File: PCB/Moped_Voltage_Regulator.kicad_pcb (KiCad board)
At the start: 2 copper layers, 42.4 x 32.4 mm, 15 parts, among them J1 Screw_Terminal_01x02, J2 Screw_Terminal_01x02, Q1 IRLZ44N, Q2 IRLZ44N

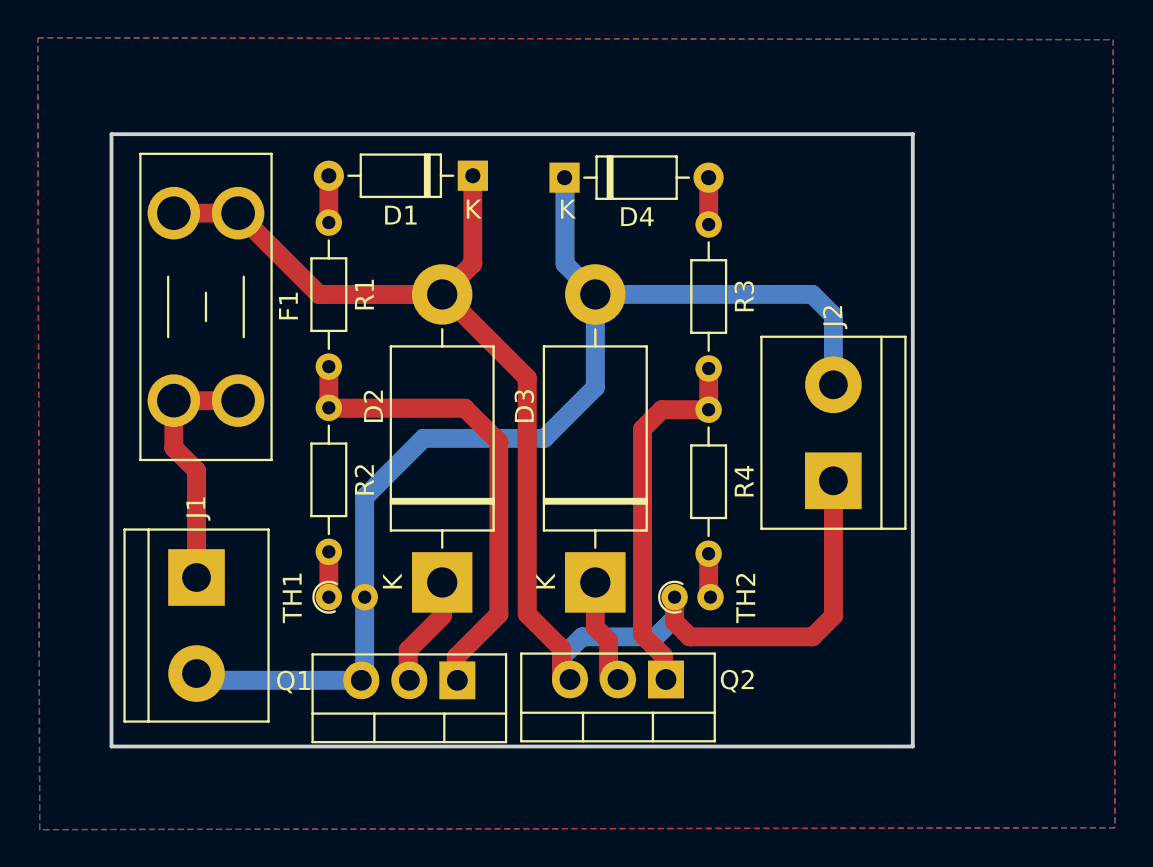
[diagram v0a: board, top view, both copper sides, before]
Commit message: Updated schematic and PCB
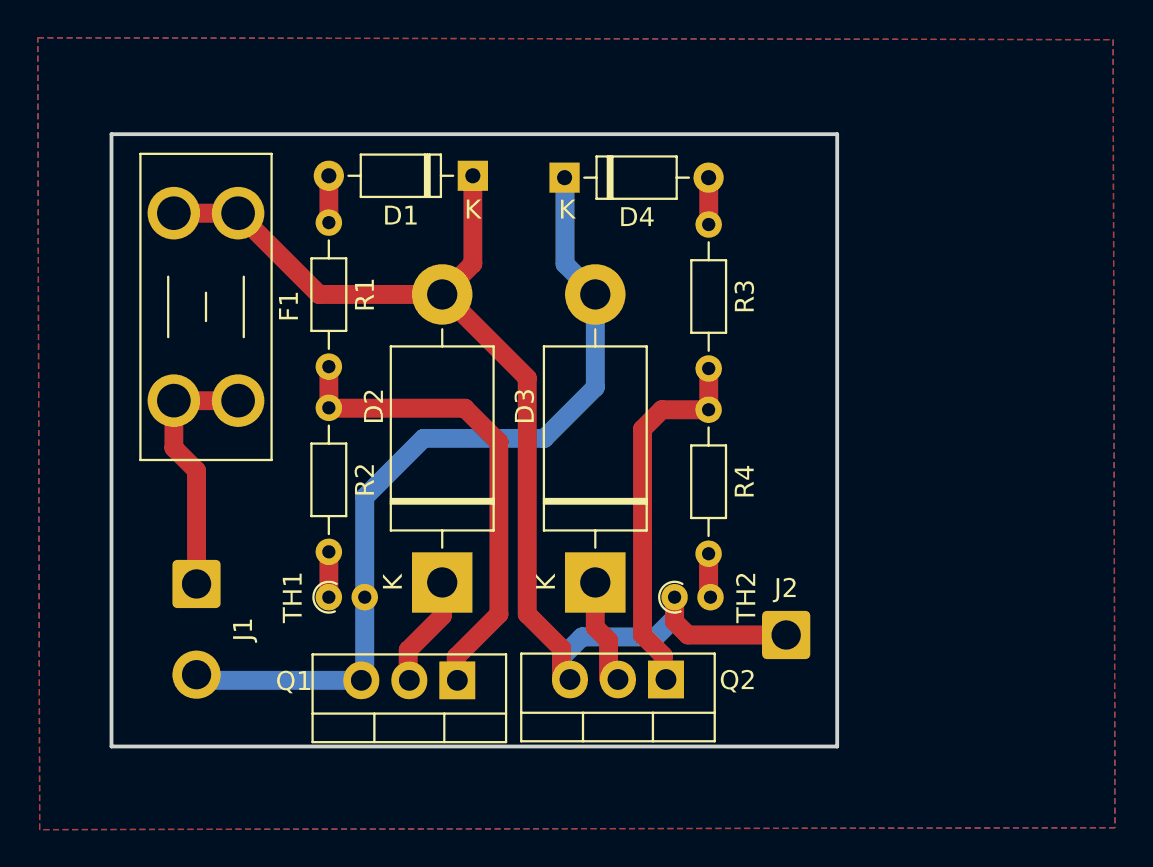
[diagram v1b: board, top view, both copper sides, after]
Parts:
- J1: value Screw_Terminal_01x02 -> Conn_01x02_Socket; footprint TerminalBlock:TerminalBlock_bornier-2_P5.08mm -> Connector_Wire:SolderWire-0.75sqmm_1x02_P4.8mm_D1.25mm_OD2.3mm
- J2: value Screw_Terminal_01x02 -> Conn_01x01_Socket; footprint TerminalBlock:TerminalBlock_bornier-2_P5.08mm -> Connector_Wire:SolderWire-0.75sqmm_1x01_D1.25mm_OD2.3mm
- moved J2 8.53 mm to (163.8, 120.3), turned to 0 degrees
- moved J1 0.34 mm to (132.6, 117.6)
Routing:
- net Earth: track 61.7 -> 45.0 mm
- net 6VAC: track 72.7 -> 63.0 mm
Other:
- board size 42.4 x 32.4 mm -> 38.4 x 32.4 mm
